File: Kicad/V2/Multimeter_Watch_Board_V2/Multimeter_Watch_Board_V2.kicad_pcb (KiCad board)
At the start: 4 copper layers, 0 parts

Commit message: pcb 46x46 area feasibility test (pre dimensions reduction)
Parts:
- added BT1: Some Li-Po?, Connector_Molex:Molex_PicoBlade_53047-0210_1x02_P1.25mm_Vertical, F.Cu at (140.5, 78.5)
- added C1: 100n, Capacitor_SMD:C_0603_1608Metric_Pad1.05x0.95mm_HandSolder, F.Cu at (114.8, 79.2)
- added C2: 100n, Capacitor_SMD:C_0603_1608Metric_Pad1.05x0.95mm_HandSolder, F.Cu at (114.8, 76.7)
- added C3: 100n, Capacitor_SMD:C_0603_1608Metric_Pad1.05x0.95mm_HandSolder, F.Cu at (110.4, 79.2)
- added C4: 47p, Capacitor_SMD:C_0805_2012Metric_Pad1.15x1.40mm_HandSolder, F.Cu at (120.6, 73.7)
- added C5: 47p, Capacitor_SMD:C_0805_2012Metric_Pad1.15x1.40mm_HandSolder, F.Cu at (140.1, 72.9)
- added C6: 10n, Capacitor_SMD:C_0603_1608Metric_Pad1.05x0.95mm_HandSolder, F.Cu at (110.4, 76.7)
- added C7: 10u, Capacitor_SMD:C_0603_1608Metric_Pad1.05x0.95mm_HandSolder, F.Cu at (114.8, 74.2)
- added CPU1: LGT8F328P-QFP32L, Package_QFP:TQFP-32_7x7mm_P0.8mm, F.Cu at (128.5, 87.0)
- added F1: Fuse, Fuse:Fuse_0805_2012Metric_Pad1.15x1.40mm_HandSolder, F.Cu at (125.4, 71.0)
- added H1: MountingHole, MountingHole:MountingHole_2.1mm, F.Cu at (107.3, 65.0)
- added H2: MountingHole, MountingHole:MountingHole_2.1mm, F.Cu at (142.6, 65.0)
- added H3: MountingHole, MountingHole:MountingHole_2.1mm, F.Cu at (107.3, 97.5)
- added H4: MountingHole, MountingHole:MountingHole_2.1mm, F.Cu at (142.6, 97.5)
- added J1: S3B-PH-K-S(LF)(SN), Multimeter_Watch_Custom_Footprints:JST_S3B-PH-K-S(LF)(SN), F.Cu at (135.5, 64.5)
- added J2: S3B-PH-K-S(LF)(SN), Multimeter_Watch_Custom_Footprints:JST_S3B-PH-K-S(LF)(SN), F.Cu at (123.5, 64.5)
- added J3: S3B-PH-K-S(LF)(SN), Multimeter_Watch_Custom_Footprints:JST_S3B-PH-K-S(LF)(SN), F.Cu at (115.0, 64.5)
- added J6: 51281-1294, Multimeter_Watch_Custom_Footprints:Molex-51281-1294-Manufacturer_Recommended, F.Cu at (124.5, 96.0)
- added J7: Conn_01x11_Female, Connector_PinSocket_2.54mm:PinSocket_1x11_P2.54mm_Vertical, F.Cu at (104.0, 68.5)
- added J8: Conn_01x11_Female, Connector_PinSocket_2.54mm:PinSocket_1x11_P2.54mm_Vertical, F.Cu at (146.0, 68.5)
- added R1: 1M, Resistor_SMD:R_0805_2012Metric_Pad1.15x1.40mm_HandSolder, F.Cu at (120.6, 69.4)
- added R10: 680, Resistor_SMD:R_0603_1608Metric_Pad1.05x0.95mm_HandSolder, F.Cu at (120.4, 79.2)
- added R11: 4k7, Resistor_SMD:R_0603_1608Metric_Pad1.05x0.95mm_HandSolder, F.Cu at (124.8, 79.2)
- added R12: 4k7, Resistor_SMD:R_0603_1608Metric_Pad1.05x0.95mm_HandSolder, F.Cu at (129.1, 79.2)
- added R13: 1M, Resistor_SMD:R_0603_1608Metric_Pad1.05x0.95mm_HandSolder, F.Cu at (110.4, 71.7)
- added R14: 1M, Resistor_SMD:R_0603_1608Metric_Pad1.05x0.95mm_HandSolder, F.Cu at (114.8, 71.7)
- added R15: 30, Resistor_SMD:R_2512_6332Metric_Pad1.52x3.35mm_HandSolder, F.Cu at (146.0, 62.0)
- added R16: 30, Resistor_SMD:R_2512_6332Metric_Pad1.52x3.35mm_HandSolder, F.Cu at (104.0, 62.0)
- added R17: 200, Resistor_SMD:R_0805_2012Metric_Pad1.15x1.40mm_HandSolder, F.Cu at (135.4, 77.2)
- added R18: 200, Resistor_SMD:R_0805_2012Metric_Pad1.15x1.40mm_HandSolder, F.Cu at (130.1, 74.0)
- added R19: 1k, Resistor_SMD:R_0805_2012Metric_Pad1.15x1.40mm_HandSolder, F.Cu at (125.4, 74.0)
- added R2: 100k, Resistor_SMD:R_0805_2012Metric_Pad1.15x1.40mm_HandSolder, F.Cu at (125.4, 68.1)
- added R20: 1k, Resistor_SMD:R_0805_2012Metric_Pad1.15x1.40mm_HandSolder, F.Cu at (130.1, 71.0)
- added R21: 10k, Resistor_SMD:R_0603_1608Metric_Pad1.05x0.95mm_HandSolder, F.Cu at (124.8, 76.7)
- added R3: 1.43M, Resistor_SMD:R_0805_2012Metric_Pad1.15x1.40mm_HandSolder, F.Cu at (130.1, 68.1)
- added R4: 100k, Resistor_SMD:R_0805_2012Metric_Pad1.15x1.40mm_HandSolder, F.Cu at (135.4, 71.2)
- added R5: 1M, Resistor_SMD:R_0805_2012Metric_Pad1.15x1.40mm_HandSolder, F.Cu at (135.4, 74.2)
- added R6: 100m, Resistor_SMD:R_2512_6332Metric_Pad1.52x3.35mm_HandSolder, F.Cu at (127.5, 62.0)
- added R7: 470k, Resistor_SMD:R_0603_1608Metric_Pad1.05x0.95mm_HandSolder, F.Cu at (110.4, 74.2)
- added R8: 680, Resistor_SMD:R_0603_1608Metric_Pad1.05x0.95mm_HandSolder, F.Cu at (120.4, 76.7)
- added R9: 470k, Resistor_SMD:R_0603_1608Metric_Pad1.05x0.95mm_HandSolder, F.Cu at (129.1, 76.7)
- added U1: PCF85163-SO08, Package_SO:SOIC-8-N7_3.9x4.9mm_P1.27mm, F.Cu at (113.5, 88.5)
- added U2: AD8592, Package_SO:MSOP-10_3x3mm_P0.5mm, F.Cu at (141.0, 61.5)
- added Y1: 32kHz, Crystal:Crystal_SMD_3215-2Pin_3.2x1.5mm, F.Cu at (141.4, 69.8)
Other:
- board outline added: 46 x 46 mm

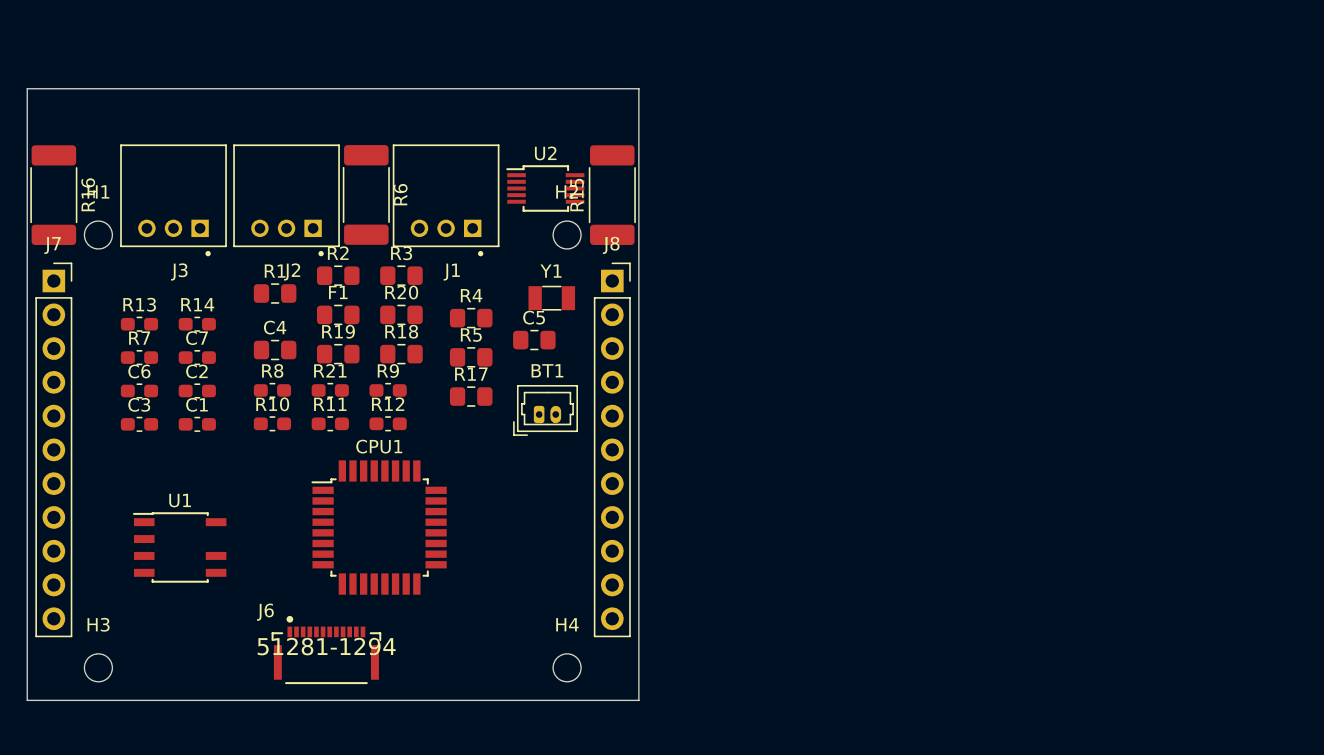
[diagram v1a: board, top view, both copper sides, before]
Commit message: shrink pcb to 46x42
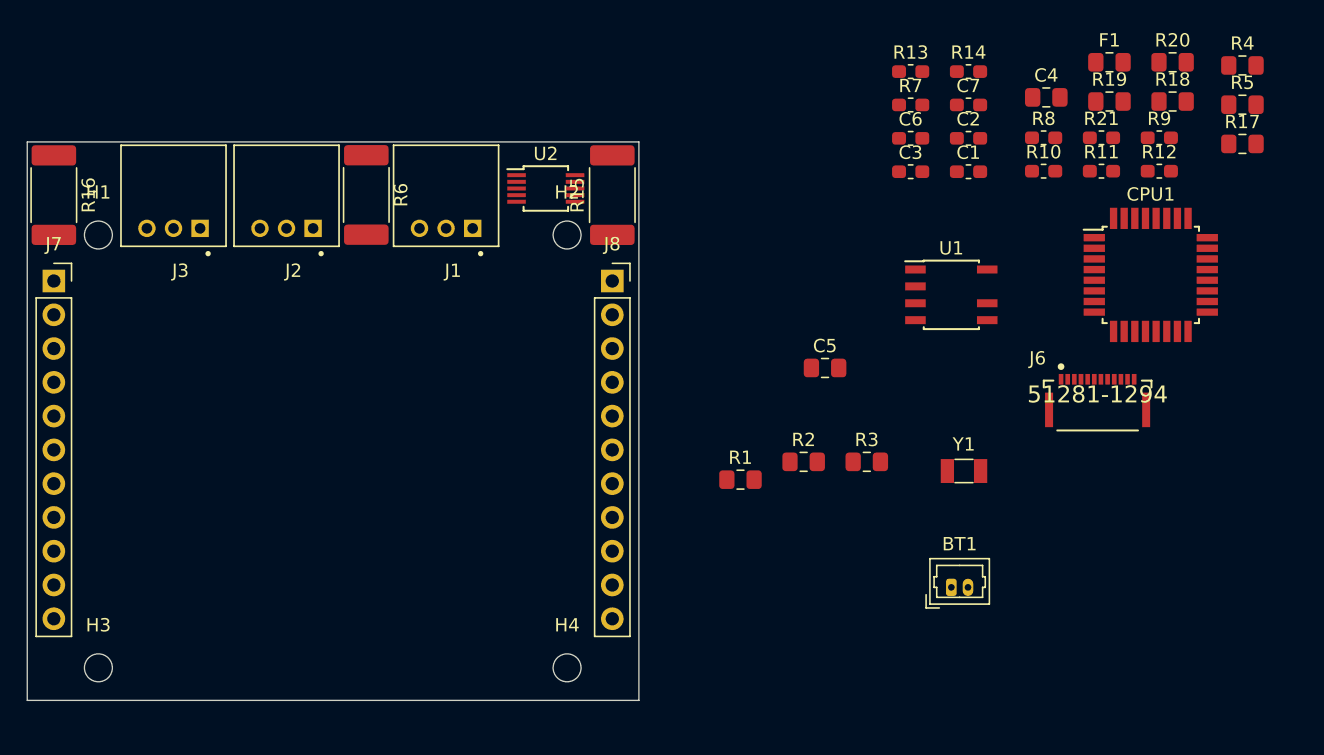
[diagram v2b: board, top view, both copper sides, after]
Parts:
- moved C3 61.0 mm to (168.4, 60.2)
- moved C6 61.0 mm to (168.4, 57.7)
- moved CPU1 61.0 mm to (186.5, 68.0)
- moved J6 61.0 mm to (182.5, 77.0)
- moved R10 61.0 mm to (178.4, 60.2)
- moved R12 61.0 mm to (187.1, 60.2)
- moved R13 61.0 mm to (168.4, 52.7)
- moved R17 61.0 mm to (193.4, 58.1)
- moved R18 61.0 mm to (188.1, 55.0)
- moved R20 61.0 mm to (188.1, 52.0)
- moved R4 61.0 mm to (193.4, 52.2)
- moved R5 61.0 mm to (193.4, 55.2)
- moved R7 61.0 mm to (168.4, 55.2)
- moved R8 61.0 mm to (178.4, 57.7)
- moved R9 61.0 mm to (187.1, 57.7)
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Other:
- board size 46 x 46 mm -> 46 x 42 mm

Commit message: wip on measuring circuits
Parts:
- moved R4 77.4 mm to (119.0, 73.5)
- moved F1 76.3 mm to (107.5, 60.0), turned to 90 degrees
- moved R5 74.5 mm to (120.5, 70.5), turned to 90 degrees
- moved J6 60.1 mm to (125.0, 94.5)
- moved R3 50.9 mm to (115.0, 73.5)
- moved R2 48.3 mm to (113.5, 70.5), turned to 270 degrees
- moved R1 43.6 mm to (115.0, 67.5), turned to 180 degrees
- moved R6 23.5 mm to (104.0, 62.0)
- moved R16 23.0 mm to (127.0, 62.0)
- moved CPU1 14.8 mm to (192.5, 81.5)
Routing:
- net /ADC1: track 0.00 -> 11.0 mm
- net Net-(F1-Pad1): track 0.00 -> 8.94 mm
- net Net-(J2-Pad2): track 0.00 -> 8.31 mm
- net Net-(J2-Pad1): track 0.00 -> 6.23 mm
- net /ADC0: track 0.00 -> 3.51 mm
- net /ADC10: track 0.00 -> 2.18 mm
- net /ADC7: track 0.00 -> 2.17 mm
- net /PD7: track 0.00 -> 2.16 mm
- net /PB0: track 0.00 -> 1.95 mm

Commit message: wip on V2 board
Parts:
- C1, C2, C3, C6, C7: footprint Capacitor_SMD:C_0603_1608Metric_Pad1.05x0.95mm_HandSolder -> Capacitor_SMD:C_0805_2012Metric_Pad1.15x1.40mm_HandSolder
- R10, R11, R12, R13, R14, R21, R7, R8, R9: footprint Resistor_SMD:R_0603_1608Metric_Pad1.05x0.95mm_HandSolder -> Resistor_SMD:R_0805_2012Metric_Pad1.15x1.40mm_HandSolder
- moved R20 88.4 mm to (108.3, 90.1), turned to 90 degrees
- moved R19 84.7 mm to (106.3, 90.1), turned to 90 degrees
- moved R21 78.1 mm to (111.5, 89.5), turned to 180 degrees
- moved CPU1 73.6 mm to (119.0, 85.0), turned to 180 degrees
- moved C7 72.1 mm to (112.4, 94.5), turned to 180 degrees
- moved R17 66.6 mm to (127.5, 67.5), turned to 180 degrees
- moved BT1 58.8 mm to (113.0, 97.8), turned to 180 degrees
- moved C1 57.1 mm to (126.0, 93.0)
- moved R9 55.8 mm to (133.5, 73.0), turned to 180 degrees
- moved Y1 55.5 mm to (118.8, 96.8), turned to 270 degrees
- moved U1 54.9 mm to (124.0, 97.0)
- moved C4 53.3 mm to (127.5, 69.5)
- moved R12 51.9 mm to (139.0, 79.5), turned to 90 degrees
- moved C6 50.5 mm to (126.5, 85.9), turned to 90 degrees
- moved C3 47.6 mm to (128.4, 85.9), turned to 90 degrees
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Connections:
- CPU1 pad 18: /SWC -> /DACout
- CPU1 pad 27: /SCL -> /SDA
- CPU1 pad 28: /SDA -> /SCL
- J1 pad 1: /ADC3_former11 -> /ADC3
- J6 pad 1: Net-(J6-Pad1) -> /PE4
- J6 pad 10: Net-(J6-Pad10) -> /GND
- J6 pad 11: Net-(J6-Pad11) -> /SDA
- J6 pad 12: Net-(J6-Pad12) -> /SCL
- J6 pad 2: Net-(J6-Pad2) -> /PD3
- J6 pad 3: Net-(J6-Pad3) -> /PD2
- J6 pad 4: Net-(J6-Pad4) -> /PE5
- J6 pad 5: Net-(J6-Pad5) -> /PB6
- J6 pad 6: Net-(J6-Pad6) -> /PB7
- J6 pad 7: Net-(J6-Pad7) -> /PD5
- J6 pad 8: Net-(J6-Pad8) -> /PD6
- J6 pad 9: Net-(J6-Pad9) -> /VCC
- J7 pad 5: /D0 -> /RESET
- J7 pad 6: /D1 -> /D0
- J7 pad 7: /RESET -> /D1
- J8 pad 6: /SCL -> /SDA
- J8 pad 7: /SDA -> /SCL
- J8 pad 9: /SWC -> /DACout
- R7 pad 2: /ADC3_former11 -> /ADC3
- R8 pad 2: /ADC3_former11 -> /ADC3
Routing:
- net /SDA: track 0.00 -> 63.7 mm, vias 0 -> 2
- net /SCL: track 0.00 -> 52.7 mm, vias 0 -> 2
- net /PD3: track 0.00 -> 40.0 mm, vias 0 -> 3
- net /ADC0: track 3.51 -> 37.7 mm, vias 0 -> 2
- net /GND: track 0.00 -> 32.4 mm, vias 0 -> 7
- net /ADC1: track 11.0 -> 40.2 mm
- net /ADC7: track 2.17 -> 29.1 mm
- net /RESET: track 0.00 -> 26.7 mm
- net /ADC2: track 0.00 -> 25.3 mm, vias 0 -> 1
- net /PB4: track 0.00 -> 24.1 mm
- net /VCC: track 0.00 -> 23.9 mm, vias 0 -> 6
- net /ADC10: track 2.18 -> 25.2 mm
- net /PB3: track 0.00 -> 22.0 mm
- net /PD4: track 0.00 -> 21.3 mm, vias 0 -> 2
- net /PB2: track 0.00 -> 20.1 mm
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- added copper zone on F.Cu, net /GND
- added copper zone on In1.Cu, net /GND
- added copper zone on In2.Cu, net /VCC

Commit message: V2 main board layout - first attempt
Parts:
- added B1: CMT-0502-75-SMT-TR, Multimeter_Watch_Custom_Footprints:CMT-0502-75-SMT-TR, F.Cu at (134.0, 77.0)
- added C8: 100n, Capacitor_SMD:C_0805_2012Metric_Pad1.15x1.40mm_HandSolder, F.Cu at (139.1, 77.9)
- added D1: D_Schottky, Diode_SMD:D_0805_2012Metric_Pad1.15x1.40mm_HandSolder, F.Cu at (139.0, 74.0)
- added Q1: A03400A N-MOS, Package_TO_SOT_SMD:SOT-23, F.Cu at (128.0, 75.0)
- added R22: 10K, Resistor_SMD:R_0805_2012Metric_Pad1.15x1.40mm_HandSolder, F.Cu at (130.0, 80.0)
- added R23: 100K, Resistor_SMD:R_0805_2012Metric_Pad1.15x1.40mm_HandSolder, F.Cu at (128.0, 78.0)
- moved R12 5.18 mm to (141.0, 84.3), turned to 270 degrees
- moved R11 2.10 mm to (143.0, 82.2), turned to 90 degrees
- moved J6 1.40 mm to (135.4, 87.2)
- moved BT1 0.60 mm to (113.0, 97.2)
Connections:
- J6 pad 1: /PE4 -> /PD3
- J6 pad 11: /SDA -> /SCL
- J6 pad 12: /SCL -> /SDA
- J6 pad 2: /PD3 -> /PE4
- J6 pad 3: /PD2 -> /PE5
- J6 pad 4: /PE5 -> /PB6
- J6 pad 5: /PB6 -> /PB7
- J6 pad 6: /PB7 -> /ADC11
- J7 pad 5: /RESET -> /D0
- J7 pad 6: /D0 -> /D1
- J7 pad 7: /D1 -> /RESET
- J8 pad 6: /SDA -> /SCL
- J8 pad 7: /SCL -> /SDA
- J8 pad 9: /DACout -> Net-(J8-Pad9)
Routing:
- net /DACout: track 14.8 -> 67.8 mm, vias 1 -> 2
- net /ADC3: track 8.21 -> 58.1 mm, vias 1 -> 2
- net /SWD: track 2.49 -> 48.9 mm
- net /ADC6: track 15.8 -> 61.6 mm, vias 1 -> 2
- net /ADC2: track 25.3 -> 68.3 mm, vias 1 -> 2
- net /ADC11: track 0.00 -> 25.9 mm, vias 0 -> 2
- net /PD3: track 40.0 -> 57.6 mm
- net /PD4: track 21.3 -> 36.7 mm
- net Net-(B1-Pad2): track 0.00 -> 12.6 mm
- net /SDA: track 63.7 -> 55.2 mm
- net /VCC: track 23.9 -> 30.2 mm, vias 6 -> 7
- net /GND: track 32.4 -> 37.9 mm, vias 7 -> 10
- net Net-(Q1-Pad1): track 0.00 -> 4.92 mm
- net /PE4: track 9.99 -> 13.8 mm
- net /PD5: track 15.3 -> 19.1 mm
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
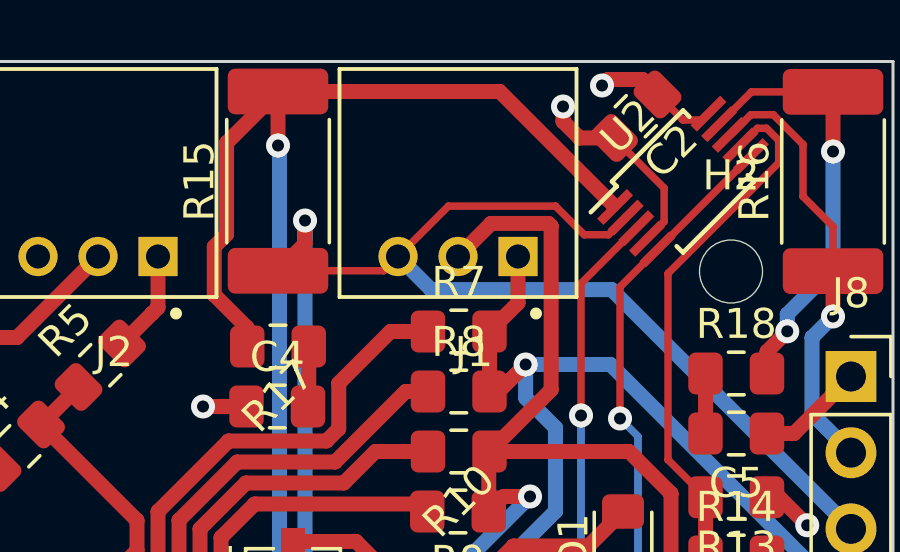
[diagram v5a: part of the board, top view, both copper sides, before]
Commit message: fix thin dacout line
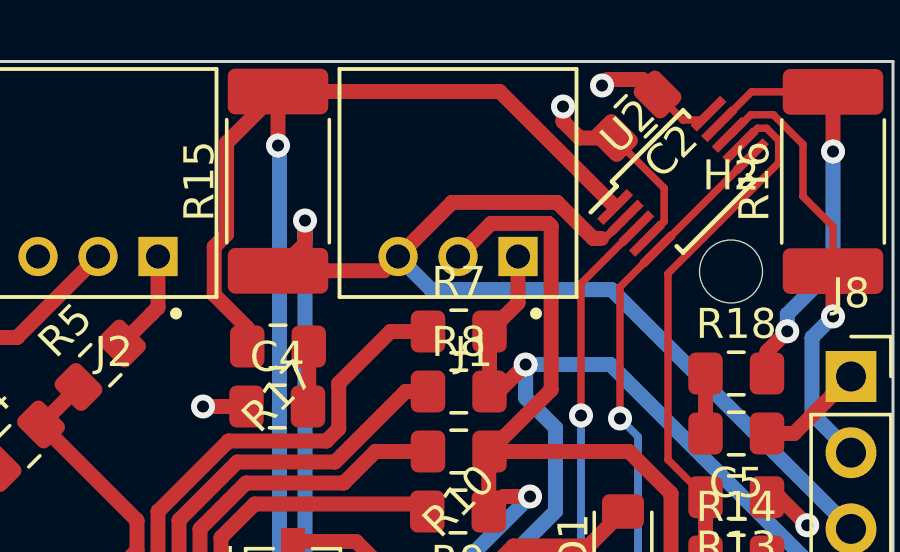
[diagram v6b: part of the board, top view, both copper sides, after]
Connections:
- J7 pad 5: /D0 -> /RESET
- J7 pad 6: /D1 -> /D0
- J7 pad 7: /RESET -> /D1
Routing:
- net /DACout: track 67.8 -> 69.1 mm
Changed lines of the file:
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@@
   (general
     (thickness 1.6)
-    (drawings 10)
-    (tracks 498)
+    (drawings 12)
+    (tracks 500)
     (zones 0)
     (modules 50)
@@
     (0 F.Cu signal)
     (1 In1.Cu signal hide)
-    (2 In2.Cu signal)
+    (2 In2.Cu signal hide)
     (31 B.Cu signal)
     (32 B.Adhes user)
@@
   )
   (setup
-    (last_trace_width 0.5)
+    (last_trace_width 0.25)
     (user_trace_width 0.23)
     (user_trace_width 0.5)
@@
       (net 29 /GND))
     (pad 7 thru_hole oval (at 0 15.24) (size 1.7 1.7) (drill 1) (layers *.Cu *.Mask)
+      (net 12 /D1))
+    (pad 6 thru_hole oval (at 0 12.7) (size 1.7 1.7) (drill 1) (layers *.Cu *.Mask)
+      (net 13 /D0))
+    (pad 5 thru_hole oval (at 0 10.16) (size 1.7 1.7) (drill 1) (layers *.Cu *.Mask)
       (net 14 /RESET))
-    (pad 6 thru_hole oval (at 0 12.7) (size 1.7 1.7) (drill 1) (layers *.Cu *.Mask)
-      (net 12 /D1))
-    (pad 5 thru_hole oval (at 0 10.16) (size 1.7 1.7) (drill 1) (layers *.Cu *.Mask)
-      (net 13 /D0))
     (pad 4 thru_hole oval (at 0 7.62) (size 1.7 1.7) (drill 1) (layers *.Cu *.Mask)
       (net 23 /VCC))
@@
       (rotate (xyz 0 0 0))
     )
+  )
+  (dimension 30 (width 0.15) (layer Dwgs.User)
+    (gr_text "30.000 mm" (at 153.4 81.3 90) (layer Dwgs.User)
+      (effects (font (size 1 1) (thickness 0.15)))
+    )
+    (feature1 (pts (xy 142.6 66.3) (xy 152.686421 66.3)))
+    (feature2 (pts (xy 142.6 96.3) (xy 152.686421 96.3)))
+    (crossbar (pts (xy 152.1 96.3) (xy 152.1 66.3)))
+    (arrow1a (pts (xy 152.1 66.3) (xy 152.686421 67.426504)))
+    (arrow1b (pts (xy 152.1 66.3) (xy 151.513579 67.426504)))
+    (arrow2a (pts (xy 152.1 96.3) (xy 152.686421 95.173496)))
+    (arrow2b (pts (xy 152.1 96.3) (xy 151.513579 95.173496)))
+  )
+  (dimension 40.5 (width 0.15) (layer Dwgs.User)
+    (gr_text "40.500 mm" (at 125 105.3) (layer Dwgs.User)
+      (effects (font (size 1 1) (thickness 0.15)))
+    )
+    (feature1 (pts (xy 145.25 77.5) (xy 145.25 104.586421)))
+    (feature2 (pts (xy 104.75 77.5) (xy 104.75 104.586421)))
+    (crossbar (pts (xy 104.75 104) (xy 145.25 104)))
+    (arrow1a (pts (xy 145.25 104) (xy 144.123496 104.586421)))
+    (arrow1b (pts (xy 145.25 104) (xy 144.123496 103.413579)))
+    (arrow2a (pts (xy 104.75 104) (xy 105.876504 104.586421)))
+    (arrow2b (pts (xy 104.75 104) (xy 105.876504 103.413579)))
   )
   (dimension 10 (width 0.15) (layer Dwgs.User)
@@
   (segment (start 123.5 66.2) (end 123.3 66.4) (width 0.5) (layer F.Cu) (net 44))
   (segment (start 123.5 64.5) (end 123.5 66.2) (width 0.5) (layer F.Cu) (net 44))
-  (segment (start 133.179011 62.820989) (end 131.5 64.5) (width 0.25) (layer F.Cu) (net 47))
-  (segment (start 136.752177 62.820989) (end 133.179011 62.820989) (width 0.25) (layer F.Cu) (net 47))
-  (segment (start 137.705767 63.774579) (end 136.752177 62.820989) (width 0.25) (layer F.Cu) (net 47))
-  (segment (start 138.518315 63.774579) (end 137.705767 63.774579) (width 0.25) (layer F.Cu) (net 47))
   (segment (start 139.090812 63.202082) (end 138.518315 63.774579) (width 0.25) (layer F.Cu) (net 47))
-  (segment (start 131.025 64.975) (end 131.5 64.5) (width 0.25) (layer F.Cu) (net 47))
-  (segment (start 127.5 64.975) (end 131.025 64.975) (width 0.25) (layer F.Cu) (net 47))
   (via (at 113.3 82.5) (size 0.8) (drill 0.4) (layers F.Cu B.Cu) (net 47))
   (segment (start 114.75 83) (end 113.8 83) (width 0.5) (layer F.Cu) (net 47))
@@
   (segment (start 131.5 64.5) (end 132.604001 65.604001) (width 0.5) (layer B.Cu) (net 47))
   (segment (start 132.604001 65.604001) (end 138.624001 65.604001) (width 0.5) (layer B.Cu) (net 47))
+  (segment (start 131.025 64.975) (end 131.5 64.5) (width 0.5) (layer F.Cu) (net 47))
+  (segment (start 127.5 64.975) (end 131.025 64.975) (width 0.5) (layer F.Cu) (net 47))
+  (segment (start 138.007544 63.899579) (end 138.287235 63.899579) (width 0.5) (layer F.Cu) (net 47))
+  (segment (start 131.5 64.5) (end 133.304011 62.695989) (width 0.5) (layer F.Cu) (net 47))
+  (segment (start 136.803954 62.695989) (end 138.007544 63.899579) (width 0.5) (layer F.Cu) (net 47))
+  (segment (start 133.304011 62.695989) (end 136.803954 62.695989) (width 0.5) (layer F.Cu) (net 47))
+  (segment (start 138.393315 63.899579) (end 138.007544 63.899579) (width 0.25) (layer F.Cu) (net 47))
+  (segment (start 139.090812 63.202082) (end 138.393315 63.899579) (width 0.25) (layer F.Cu) (net 47))
   (segment (start 137.849989 74.15001) (end 135.34999 74.15001) (width 0.5) (layer F.Cu) (net 50))
   (segment (start 139 72.999999) (end 137.849989 74.15001) (width 0.5) (layer F.Cu) (net 50))
